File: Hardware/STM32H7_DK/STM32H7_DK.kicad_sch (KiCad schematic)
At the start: 27 parts

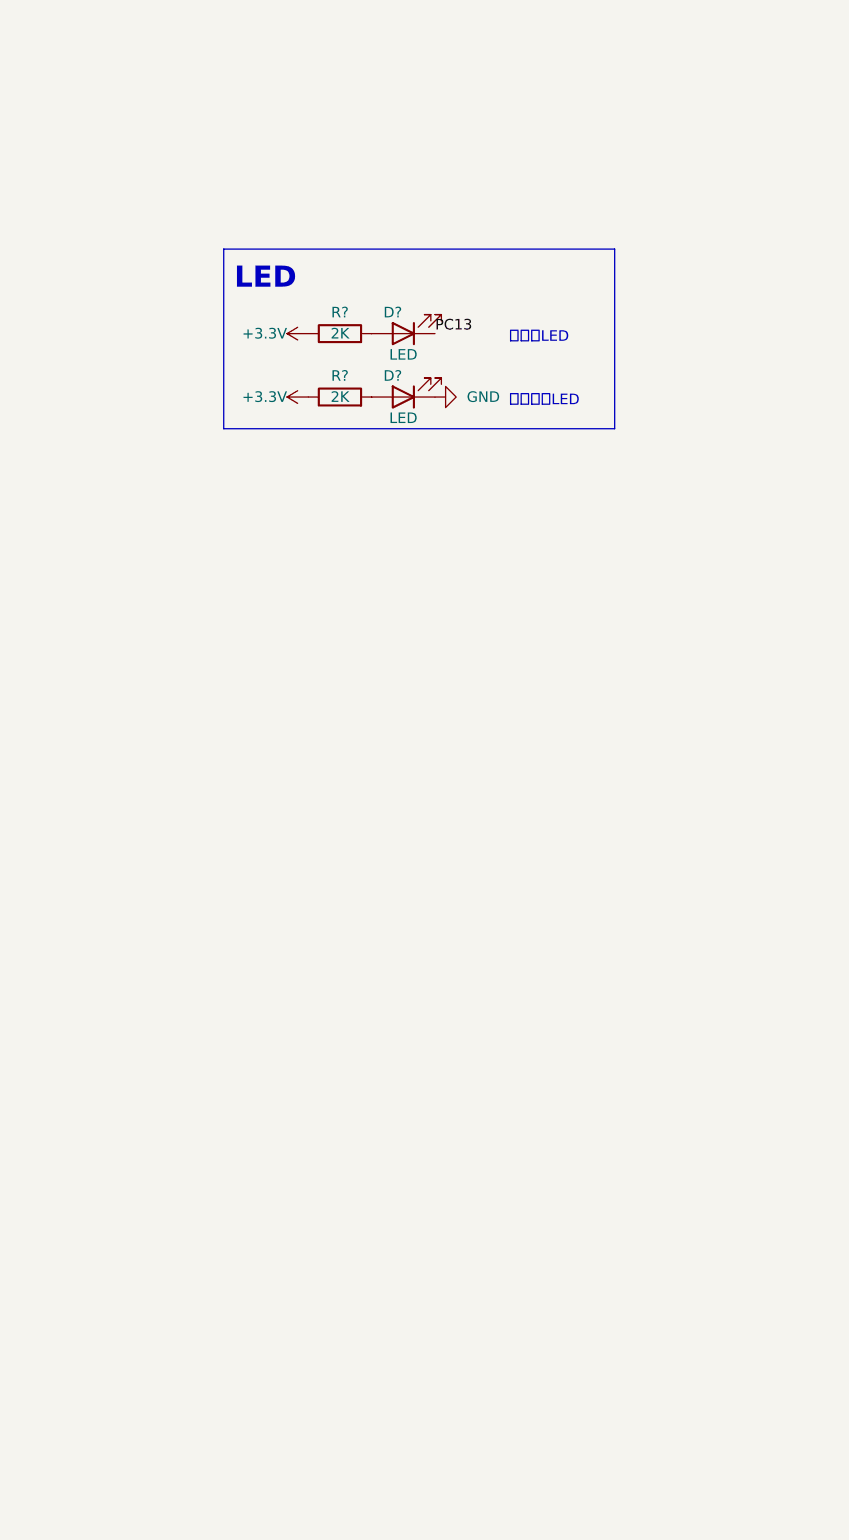
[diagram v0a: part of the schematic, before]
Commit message: STM32H7-DK开发板原理图添加TF卡座、IPS屏幕、FLASH部分
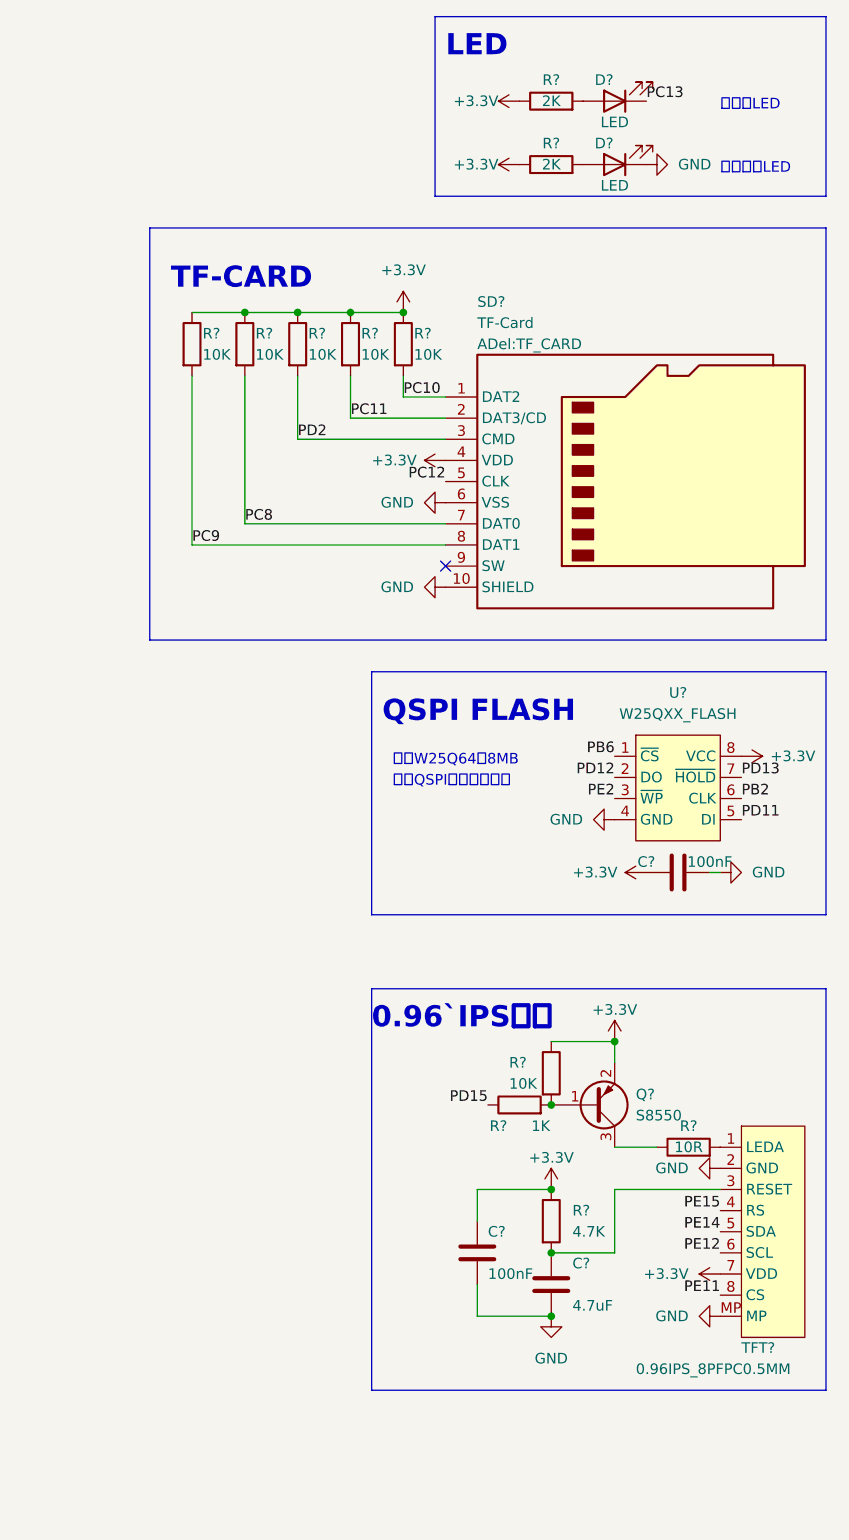
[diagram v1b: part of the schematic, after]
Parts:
- added C? (x2): 100nF, symbol Device:C
- added C?: 4.7uF, symbol Device:C
- added Q?: S8550, Package_TO_SOT_SMD:SOT-23, symbol Device:Q_PNP_BEC
- added R? (x6): 10K, symbol Device:R
- added R?: 10R, symbol Device:R
- added R?: 1K, symbol Device:R
- added R?: 4.7K, symbol Device:R
- added SD?: TF-Card, ADel:TF_CARD, symbol ADel:TF-Card
- added TFT?: 0.96IPS_8PFPC0.5MM, Connector_FFC-FPC:TE_0-1734839-8_1x08-1MP_P0.5mm_Horizontal, symbol ADel:0.96IPS_8PFPC0.5MM
- added U?: W25QXX_FLASH, symbol ADel:W25QXX_FLASH
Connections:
- net +3.3V: now also C?.1, C?.1, Q?.2 (E), R?.1, R?.1, R?.1, R?.1, R?.1, R?.1, R?.1, SD?.4 (VDD), TFT?.7 (VDD), U?.8 (VCC)
- net GND: now also C?.2, C?.2, C?.2, SD?.10 (SHIELD), SD?.6 (VSS), TFT?.2 (GND), TFT?.MP, U?.4 (GND)
- net PB2: now also U?.6 (CLK)
- net PB6: now also U?.1 (~{CS})
- net PC10: now also R?.2, SD?.1 (DAT2)
- net PC11: now also R?.2, SD?.2 (DAT3/CD)
- net PC12: now also SD?.5 (CLK)
- net PC8: now also R?.2, SD?.7 (DAT0)
- net PC9: now also R?.2, SD?.8 (DAT1)
- net PD11: now also U?.5 (DI)
- net PD12: now also U?.2 (DO)
- net PD13: now also U?.7 (~{HOLD})
- net PD15: now also R?.1
- net PD2: now also R?.2, SD?.3 (CMD)
- net PE11: now also TFT?.8 (CS)
- net PE12: now also TFT?.6 (SCL)
- net PE14: now also TFT?.5 (SDA)
- net PE15: now also TFT?.4 (RS)
- net PE2: now also U?.3 (~{WP})
- new net: Q?.3 (C), R?.1
- new net: R?.2, TFT?.1 (LEDA)
- new net: Q?.1 (B), R?.2, R?.2
- new net: C?.1, R?.2, TFT?.3 (RESET)
- no-connect marks 0 -> 1
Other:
- note added: "0.96`IPS屏幕"
- note added: "QSPI FLASH"
- note added: "TF-CARD"
- note added: "使用QSPI四线模式驱动"
- note added: "采用W25Q64，8MB"
- moved on the sheet: D?, R?

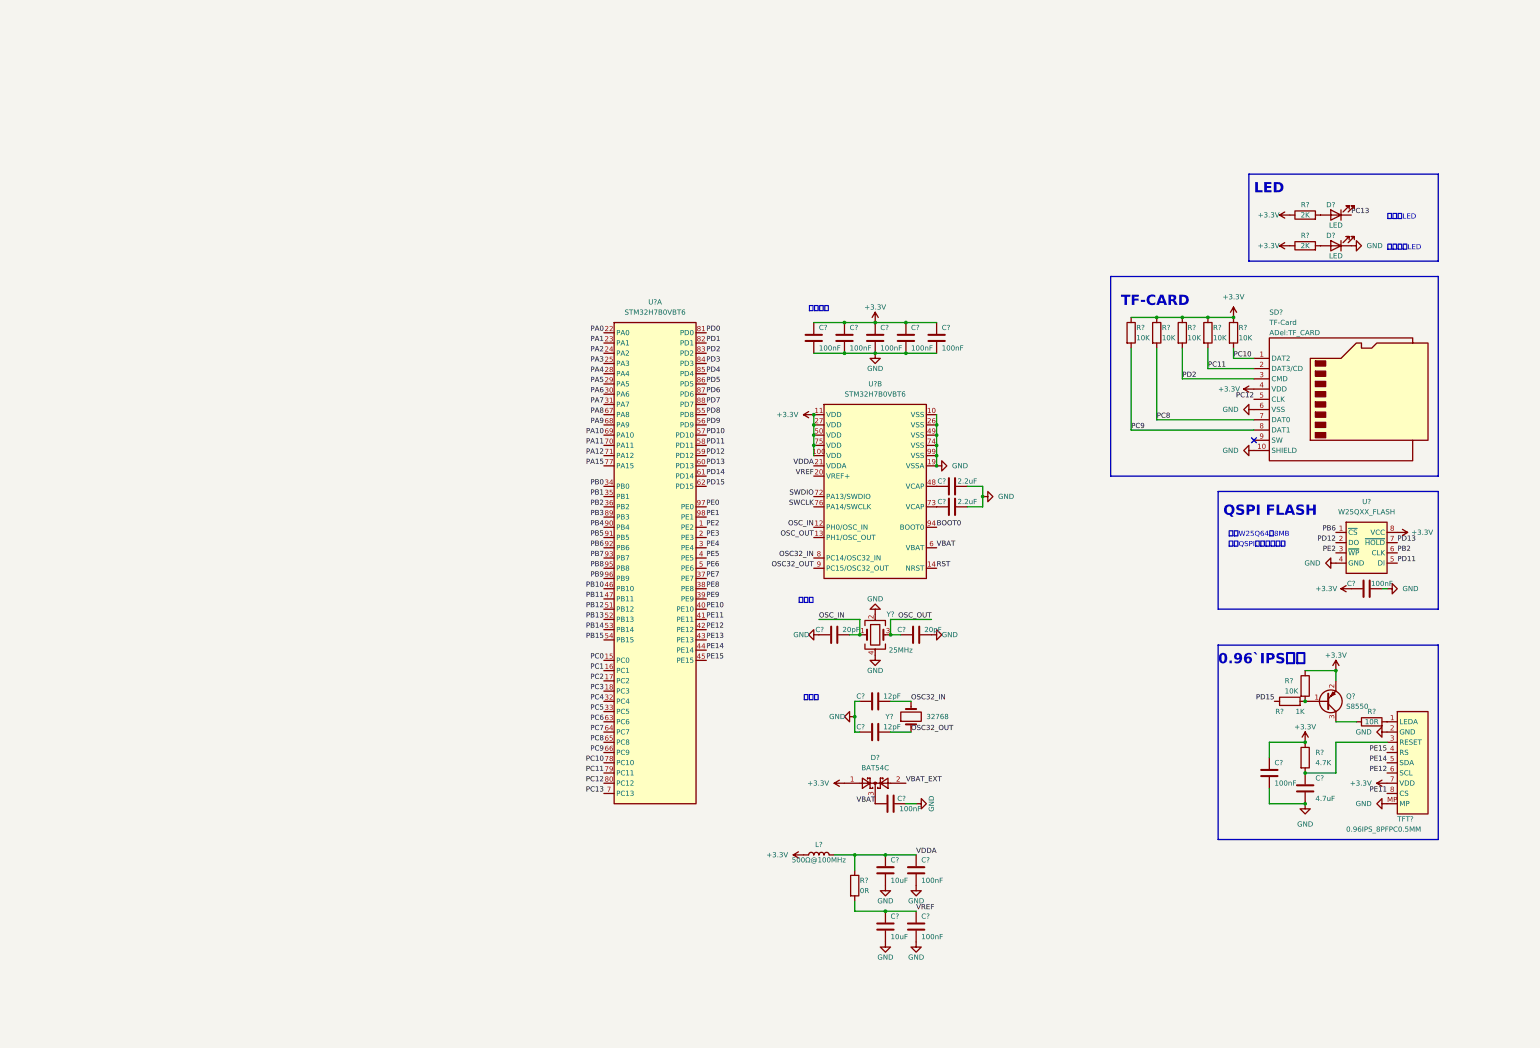
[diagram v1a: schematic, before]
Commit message: 添加原理图所有功能模块，但尚未连接节点
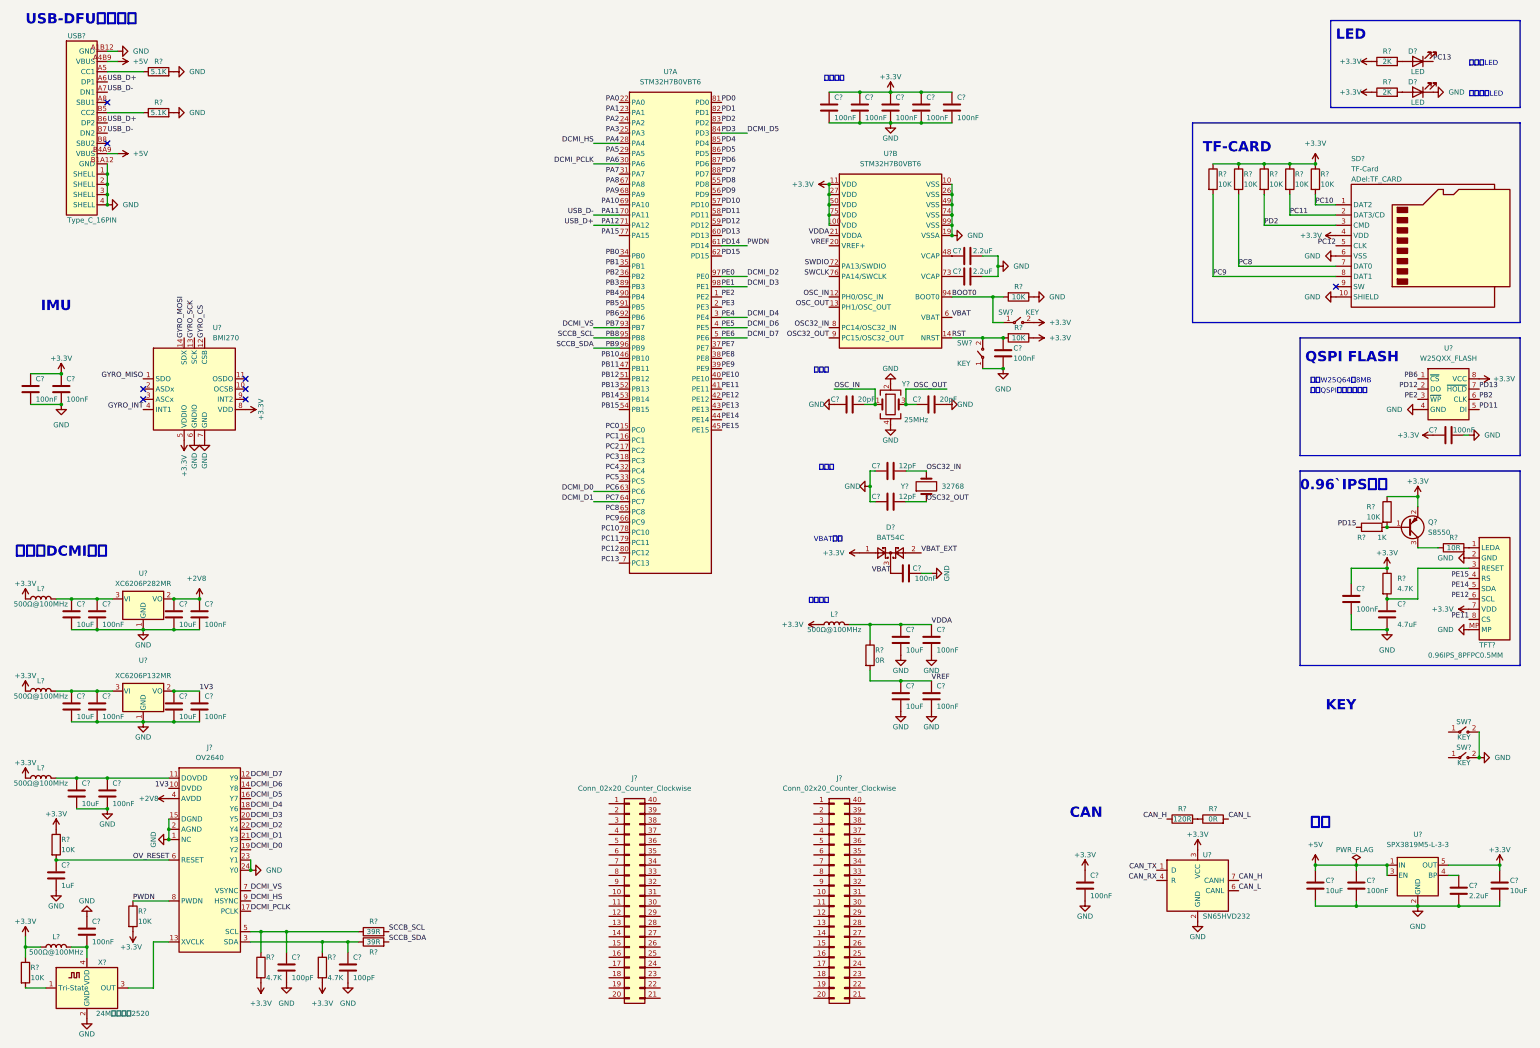
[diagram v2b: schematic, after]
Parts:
- added C? (x10): 100nF, symbol Device:C
- added C? (x5): 10uF, symbol Device:C
- added C?: 1uF, symbol Device:C
- added C? (x2): 10uF, Capacitor_SMD:C_0603_1608Metric_Pad1.08x0.95mm_HandSolder, symbol Device:C
- added C?: 100nF, Capacitor_SMD:C_0603_1608Metric_Pad1.08x0.95mm_HandSolder, symbol Device:C
- added C?: 2.2uF, Capacitor_SMD:C_0603_1608Metric_Pad1.08x0.95mm_HandSolder, symbol Device:C
- added C? (x2): 100pF, symbol Device:C
- added J? (x2): Conn_02x20_Counter_Clockwise, symbol Connector_Generic:Conn_02x20_Counter_Clockwise
- added J?: OV2640, ADel:OV2640_FPC0.5MM_24P_REVERSE, symbol ADel:OV2640
- added L? (x4): 500Ω@100MHz, symbol Device:L
- added R? (x5): 10K, symbol Device:R
- added R?: 120R, Resistor_SMD:R_0603_1608Metric_Pad0.98x0.95mm_HandSolder, symbol Device:R
- added R? (x2): 5.1K, symbol Device:R
- added R? (x2): 4.7K, symbol Device:R
- added R?: 0R, Resistor_SMD:R_0402_1005Metric, symbol Device:R
- added R? (x2): 39R, symbol Device:R
- added SW? (x4): KEY, symbol ADel:KEY
- added U?: SN65HVD232, Package_SO:SOIC-8_3.9x4.9mm_P1.27mm, symbol Interface_CAN_LIN:SN65HVD232
- added U?: XC6206P282MR, Package_TO_SOT_SMD:SOT-23, symbol Regulator_Linear:XC6206PxxxMR
- added U?: BMI270, Package_LGA:Bosch_LGA-14_3x2.5mm_P0.5mm, symbol ADel:BMI270
- added U?: XC6206P132MR, Package_TO_SOT_SMD:SOT-23, symbol Regulator_Linear:XC6206PxxxMR
- added U?: SPX3819M5-L-3-3, Package_TO_SOT_SMD:SOT-23-5, symbol Regulator_Linear:SPX3819M5-L-3-3
- added USB?: Type_C_16PIN, ADel:TYPE-C-16PIN_SMD, symbol ADel:Type_C_16PIN
- added X?: 24M有源晶振2520, Oscillator:Oscillator_SMD_ECS_2520MV-xxx-xx-4Pin_2.5x2.0mm, symbol Oscillator:ECS-2520MV-xxx-xx
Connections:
- net +3.3V: now also C?.1, C?.1, C?.1, C?.1, L?.1, L?.1, L?.1, L?.1, R?.1, R?.1, R?.1, R?.2, R?.2, R?.2, SW?.2 (B), U?.3 (VCC), U?.5 (OUT), U?.5 (VDDIO), U?.8 (VDD)
- net BOOT0: now also R?.2, SW?.1 (A)
- net GND: now also C?.1, C?.2, C?.2, C?.2, C?.2, C?.2, C?.2, C?.2, C?.2, C?.2, C?.2, C?.2, C?.2, C?.2, C?.2, C?.2, C?.2, C?.2, C?.2, C?.2, C?.2, C?.2, J?.1 (NC), J?.15 (DGND), J?.2 (AGND), J?.23 (Y1), J?.24 (Y0), R?.1, R?.2, R?.2, SW?.1 (A), SW?.2 (B), SW?.2 (B), U?.1 (GND), U?.1 (GND), U?.2 (GND), U?.2 (GND), U?.6 (GNDIO), U?.7 (GND), USB?.1 (SHELL), USB?.2 (SHELL), USB?.3 (SHELL), USB?.4 (SHELL), USB?.A1B12 (GND), USB?.B1A12 (GND), X?.2 (GND)
- net PA11: now also USB?.A7 (DN1), USB?.B7 (DN2)
- net PA12: now also USB?.A6 (DP1), USB?.B6 (DP2)
- net PB8: now also R?.2
- net PB9: now also R?.2
- net PD14: now also J?.8 (PWDN), R?.1
- net RST: now also C?.1, R?.2, SW?.2 (B)
- net PA4 renamed DCMI_HS
- net DCMI_HS: now also J?.9 (HSYNC)
- net PA6 renamed DCMI_PCLK
- net DCMI_PCLK: now also J?.17 (PCLK)
- net PB7 renamed DCMI_VS
- net DCMI_VS: now also J?.7 (VSYNC)
- net PC6 renamed DCMI_D0
- net DCMI_D0: now also J?.19 (Y2)
- net PC7 renamed DCMI_D1
- net DCMI_D1: now also J?.21 (Y3)
- net PD3 renamed DCMI_D5
- net DCMI_D5: now also J?.16 (Y7)
- net PE0 renamed DCMI_D2
- net DCMI_D2: now also J?.22 (Y4)
- net PE1 renamed DCMI_D3
- net DCMI_D3: now also J?.20 (Y5)
- net PE4 renamed DCMI_D4
- net DCMI_D4: now also J?.18 (Y6)
- net PE5 renamed DCMI_D6
- net DCMI_D6: now also J?.14 (Y8)
- net PE6 renamed DCMI_D7
- net DCMI_D7: now also J?.12 (Y9)
- new net: R?.1, R?.2
- new net: C?.1, C?.1, L?.2, U?.3 (VI) (x2)
- new net: R?.1, USB?.A5 (CC1)
- new net: C?.1, C?.1, J?.11 (DOVDD), L?.2
- new net: C?.1, J?.5 (SCL), R?.1, R?.1
- new net: R?.1, USB?.B5 (CC2)
- new net: C?.1, U?.4 (BP)
- new net: C?.1, J?.3 (SDA), R?.1, R?.1
- new net: R?.2, X?.1 (Tri-State)
- new net: C?.2, L?.2, X?.4 (VDD)
- new net: J?.13 (XVCLK), X?.3 (OUT)
- new net +2V8: C?.1, C?.1, J?.4 (AVDD), U?.2 (VO)
- new net +5V: C?.1, C?.1, U?.1 (IN), U?.3 (EN), USB?.A4B9 (VBUS), USB?.B4A9 (VBUS)
- new net 1V3: C?.1, C?.1, J?.10 (DVDD), U?.2 (VO)
- new net CAN_H: R?.1, U?.7 (CANH)
- new net CAN_L: R?.2, U?.6 (CANL)
- new net CAN_RX: U?.4 (R)
- new net CAN_TX: U?.1 (D)
- new net GYRO_CS: U?.12 (CSB)
- new net GYRO_INT: U?.4 (INT1)
- new net GYRO_MISO: U?.1 (SDO)
- new net GYRO_MOSI: U?.14 (SDX)
- new net GYRO_SCK: U?.13 (SCK)
- new net OV_RESET: C?.1, J?.6 (RESET), R?.2
- no-connect marks 1 -> 8
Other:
- note added: "CAN"
- note added: "IMU"
- note added: "KEY"
- note added: "USB-DFU下载模式"
- note added: "VBAT电源"
- note added: "摄像头DCMI接口"
- note added: "模拟电源"
- note added: "电源"
- moved on the sheet: C?, D?, L?, Q?, R?, SD?, TFT?, U?, U?A, U?B, Y?

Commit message: 尝试H7PCB布局，大量未连接端
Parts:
- removed R?: 0R, Resistor_SMD:R_0402_1005Metric, symbol Device:R
- added J4: Conn_01x02_Male, ADel:SH1.0_01x02P_WT, symbol Connector:Conn_01x02_Male
- C1, C10, C11, C12, C13, C14, C15, C16, C17, C19, C2, C20, C23, C24, C25, C26, C28, C29, C3, C30, C31, C32, C33, C34, C36, C38, C39, C4, C5, C6, C7, C8, C9: renamed from C?; footprint (none) -> Capacitor_SMD:C_0603_1608Metric_Pad1.08x0.95mm_HandSolder
- D2, D3: renamed from D?; footprint (none) -> LED_SMD:LED_0603_1608Metric_Pad1.05x0.95mm_HandSolder
- J2, J3: renamed from J?; footprint (none) -> Connector_PinSocket_2.54mm:PinSocket_2x20_P2.54mm_Vertical
- L1, L2, L3, L4, L5: renamed from L?; footprint (none) -> Inductor_SMD:L_0603_1608Metric_Pad1.05x0.95mm_HandSolder
- R1, R10, R11, R12, R14, R16, R17, R18, R19, R2, R20, R21, R22, R23, R24, R25, R3, R4, R5, R6, R7, R8, R9: renamed from R?; footprint (none) -> Resistor_SMD:R_0603_1608Metric_Pad0.98x0.95mm_HandSolder
- SW1, SW2, SW3, SW4: renamed from SW?; footprint (none) -> ADel:SW_3x4
- U4: renamed from U?; footprint (none) -> Package_QFP:LQFP-100_14x14mm_P0.5mm
- U7: renamed from U?; footprint (none) -> Package_SO:SOIC-8_3.9x4.9mm_P1.27mm
- Y2: renamed from Y?; footprint (none) -> Crystal:Crystal_SMD_MicroCrystal_CM9V-T1A-2Pin_1.6x1.0mm_HandSoldering
- gave numbers to parts that had none: 22
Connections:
- net PB12 is gone; now on net CAN_RX: U4.51 (PB12)
- net PB13 is gone; now on net CAN_TX: U4.52 (PB13)
- net CAN_H: now also J4.2 (Pin_2)
- net CAN_L: now also R13.2, J4.1 (Pin_1)
- net KEY_B: now reaches SW4.1 (A)
- net KEY_A: now reaches SW3.1 (A)
- no-connect marks 8 -> 88
